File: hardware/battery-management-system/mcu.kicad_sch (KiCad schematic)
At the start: 44 parts, among them J13 I2C, J14 UART_INTERCONNECT, J15 LEDS, J16 CHARGE/DISCHARGE, J17 UART_USB, Q5 DMN3404L, U10 STM32L071CZTx, U6 ARM-JTAG-SWD, U7 AT24C512C, U8 NCT75DR2G, U9 STC3100

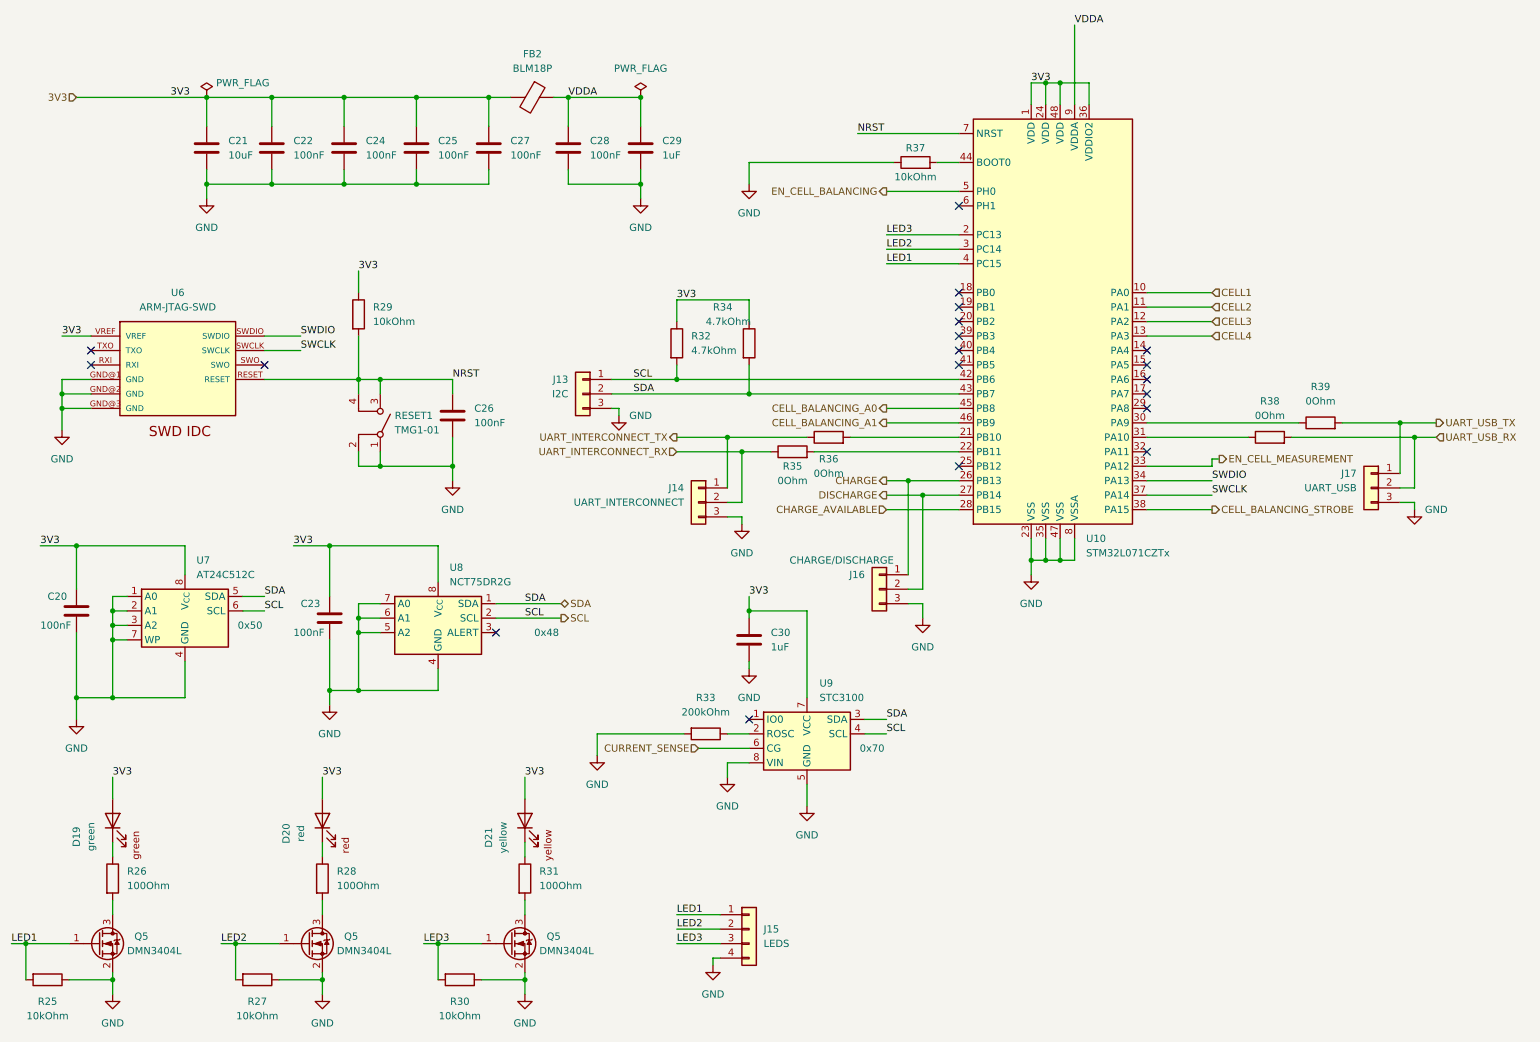
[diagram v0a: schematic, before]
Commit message: start simplifying BMS for R02
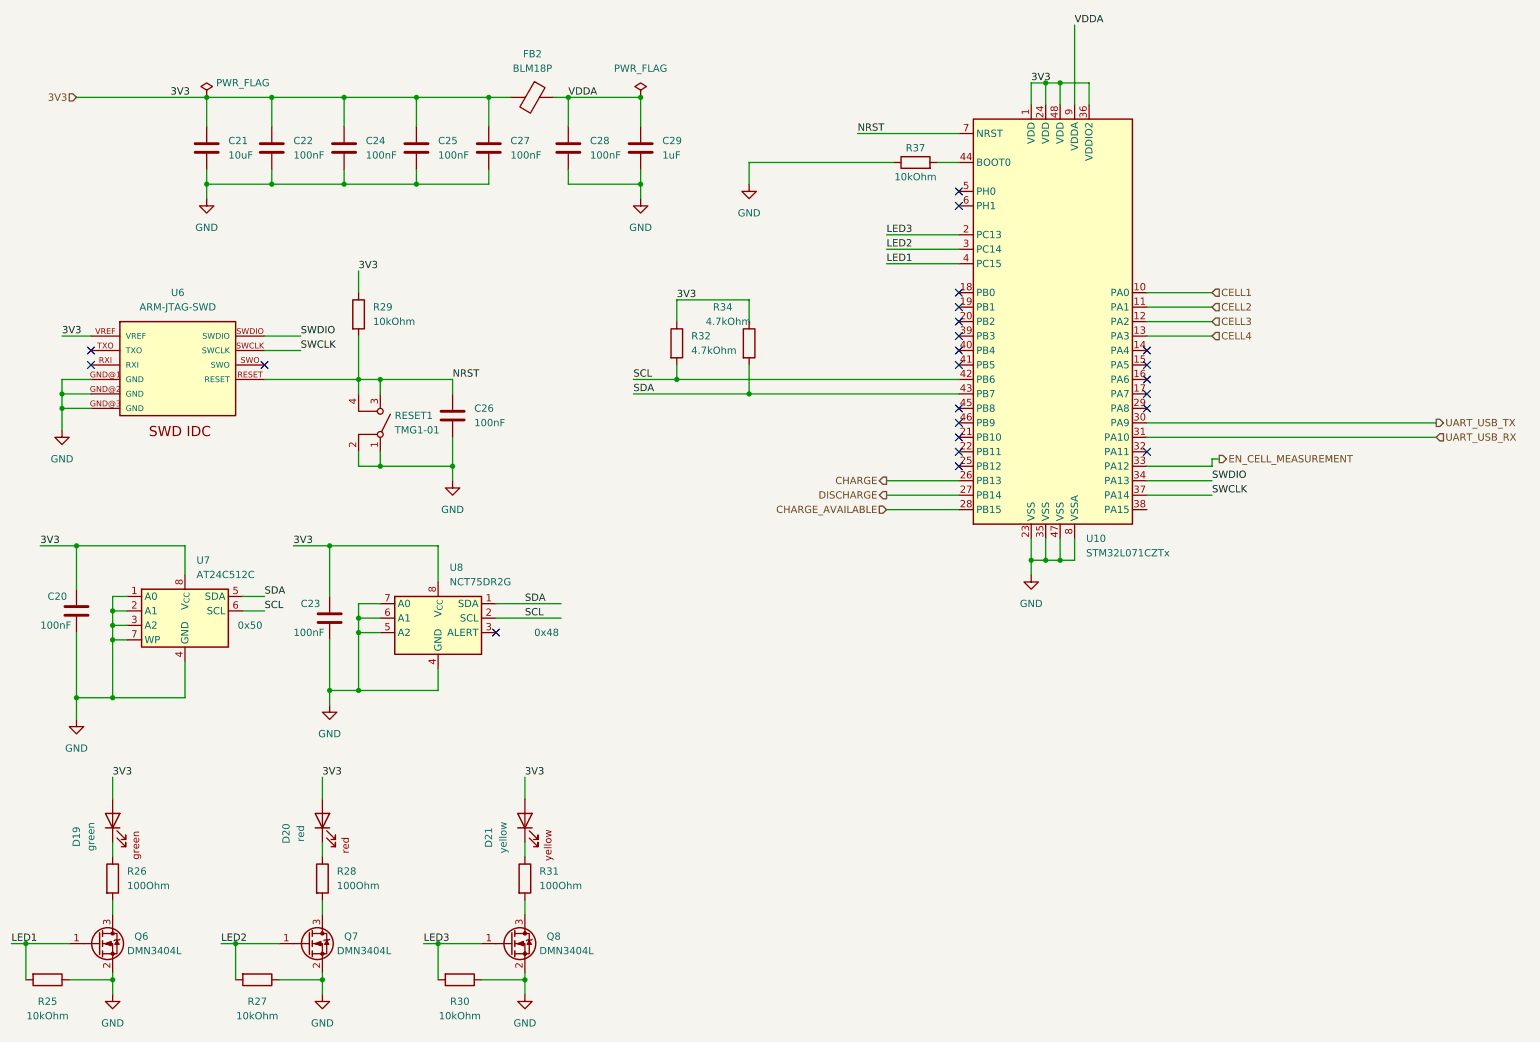
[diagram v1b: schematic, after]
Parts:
- removed C30: 1uF, benediktibk:C_0603_1608Metric_Pad1.08x0.95mm_HandSolder, symbol benediktibk:C_1uF_SMD_0603_50V_10%
- removed J13: I2C, benediktibk:PinHeader_1x03_P2.54mm_Vertical, symbol benediktibk:Conn_01x03
- removed J14: UART_INTERCONNECT, benediktibk:PinHeader_1x03_P2.54mm_Vertical, symbol benediktibk:Conn_01x03
- removed J15: LEDS, benediktibk:PinHeader_1x04_P2.54mm_Vertical, symbol benediktibk:Conn_01x04
- removed J16: CHARGE/DISCHARGE, benediktibk:PinHeader_1x03_P2.54mm_Vertical, symbol benediktibk:Conn_01x03
- removed J17: UART_USB, benediktibk:PinHeader_1x03_P2.54mm_Vertical, symbol benediktibk:Conn_01x03
- removed R33: 200kOhm, benediktibk:R_0603_1608Metric_Pad0.98x0.95mm_HandSolder, symbol benediktibk:R_200kOhm_SMD_0603_30mW_0_1%
- removed R35, R36, R38, R39: 0Ohm, benediktibk:R_0603_1608Metric_Pad0.98x0.95mm_HandSolder, symbol benediktibk:R_0Ohm_SMD_0603_100mW_0%
- removed U9: STC3100, benediktibk:MSOP-8_3x3mm_P0.65mm, symbol benediktibk:STC3100
- renumbered Q5 to Q6, Q5 to Q7, Q5 to Q8
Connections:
- net UART_USB_RX: now also U10.31 (PA10)
- net UART_USB_TX: now also U10.30 (PA9)
- net CELL_BALANCING_A0: no longer names the net of U10.45 (PB8)
- net CELL_BALANCING_A1: no longer names the net of U10.46 (PB9)
- net CELL_BALANCING_STROBE: no longer names the net of U10.38 (PA15)
- net EN_CELL_BALANCING: no longer names the net of U10.5 (PH0)
- no-connect marks 19 -> 23

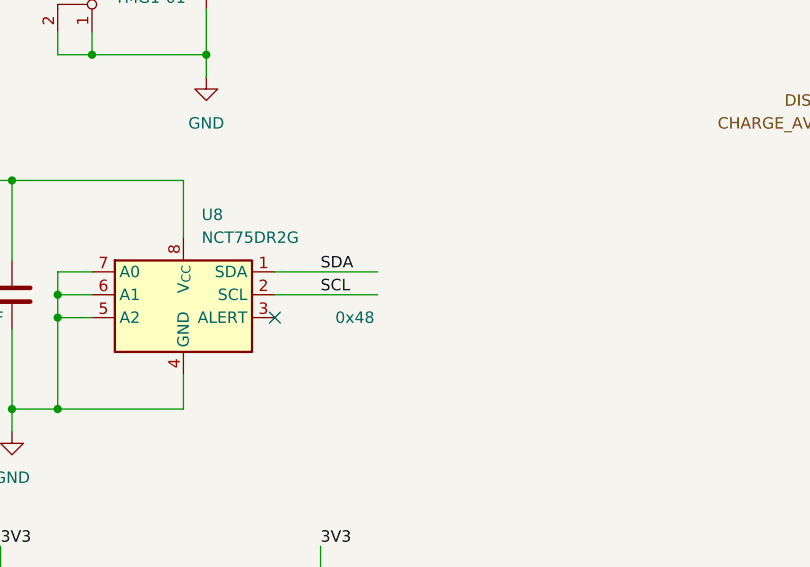
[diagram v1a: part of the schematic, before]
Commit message: update PCB from schematic
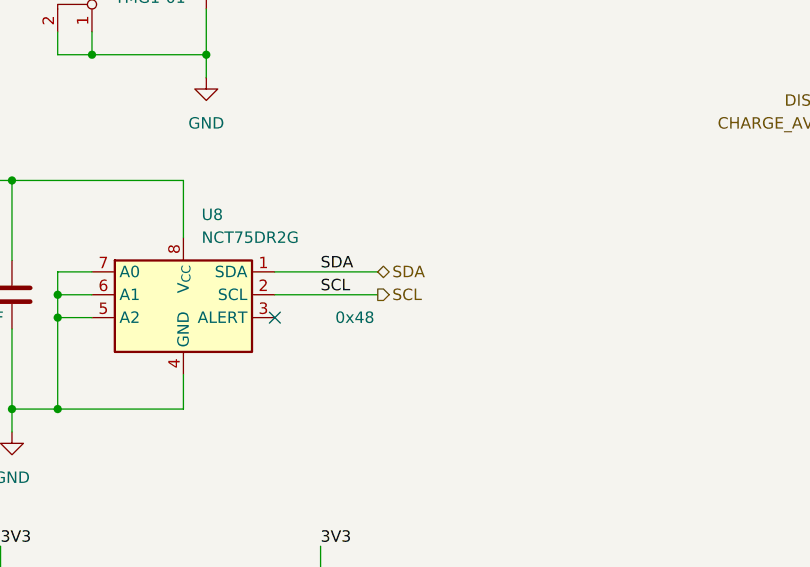
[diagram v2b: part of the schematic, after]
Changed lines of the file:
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@@
+    (effects (font (size 1.27 1.27)) (justify left))
+  )
+  (hierarchical_label "SCL" (shape output) (at 115.57 123.19 0) (fields_autoplaced)
+    (effects (font (size 1.27 1.27)) (justify left))
+  )
+  (hierarchical_label "SDA" (shape bidirectional) (at 115.57 120.65 0) (fields_autoplaced)
     (effects (font (size 1.27 1.27)) (justify left))
   )

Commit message: fix design errors
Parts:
- renumbered D19 to D17, D20 to D18, D21 to D19, R25 to R23, R26 to R24, R27 to R25, R28 to R26, R29 to R27, R30 to R28, R31 to R29, R32 to R30, R34 to R31, R37 to R32, U10 to U9

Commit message: fix design errors
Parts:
- J7: renamed from U6; footprint benediktibk:ARM-JTAG-10-SWD-IDC -> benediktibk:SAMTEC_FTSH-105-01-F-DV-P-TR
- renumbered D17 to D15, D18 to D16, D19 to D17, U7 to U6, U8 to U7, U9 to U8
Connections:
- net 3V3: now also J7.01 (VCC); no longer J7.VREF
- net GND: now also J7.03 (GND), J7.05 (GND), J7.09 (GND); no longer J7.GND@1 (GND), J7.GND@2 (GND), J7.GND@3 (GND)
- net NRST: now also J7.10 (RESET); no longer J7.RESET
- net SWCLK: now also J7.04 (SWCLK); no longer J7.SWCLK
- net SWDIO: now also J7.02 (SWDIO); no longer J7.SWDIO
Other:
- moved on the sheet: C26, RESET1

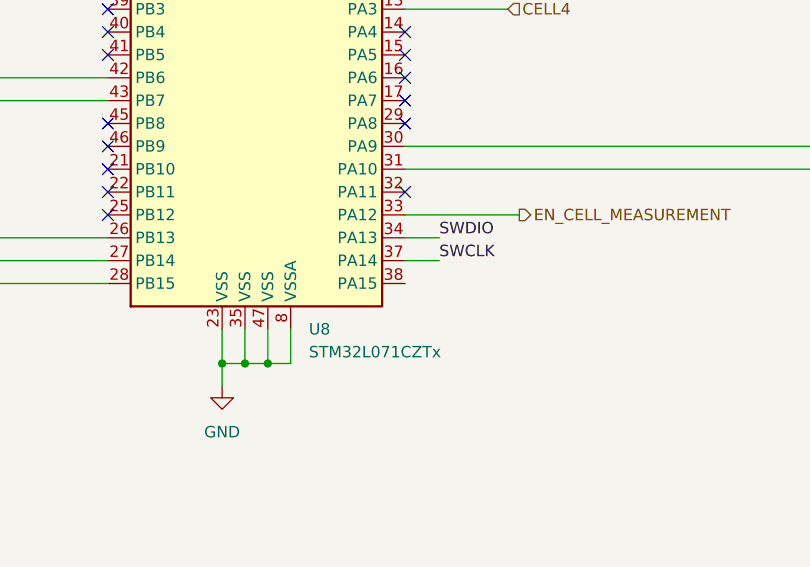
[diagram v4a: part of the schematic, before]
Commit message: add heatsink and fix ERC errors
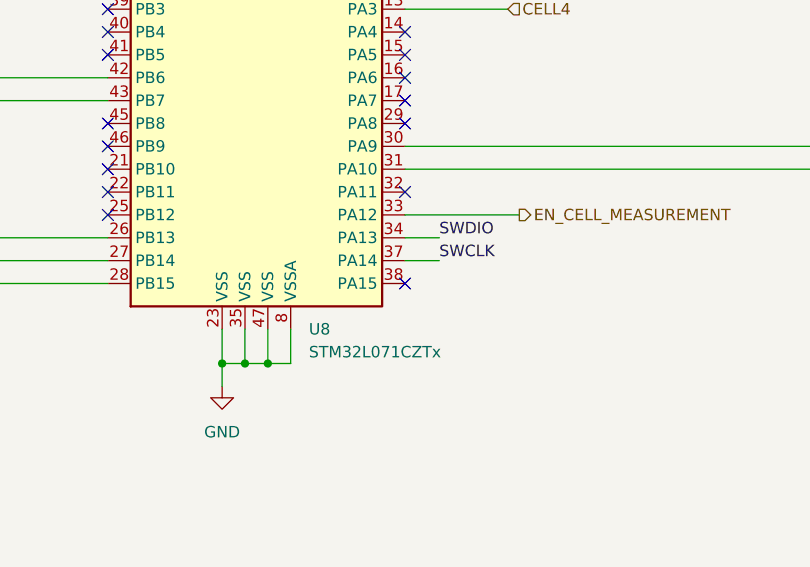
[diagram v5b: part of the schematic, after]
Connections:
- no-connect marks 23 -> 24
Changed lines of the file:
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@@
   (no_connect (at 185.42 93.98))
   (no_connect (at 218.44 81.28))
+  (no_connect (at 218.44 104.14))
   (no_connect (at 185.42 91.44))
   (no_connect (at 53.34 81.28))
